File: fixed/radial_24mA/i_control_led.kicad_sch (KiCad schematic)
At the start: 14 parts, among them J1 Conn_01x04, J2 Conn_01x04, Q1 MMBT5551L, U1 TPS61222DCK, U2 LMV321

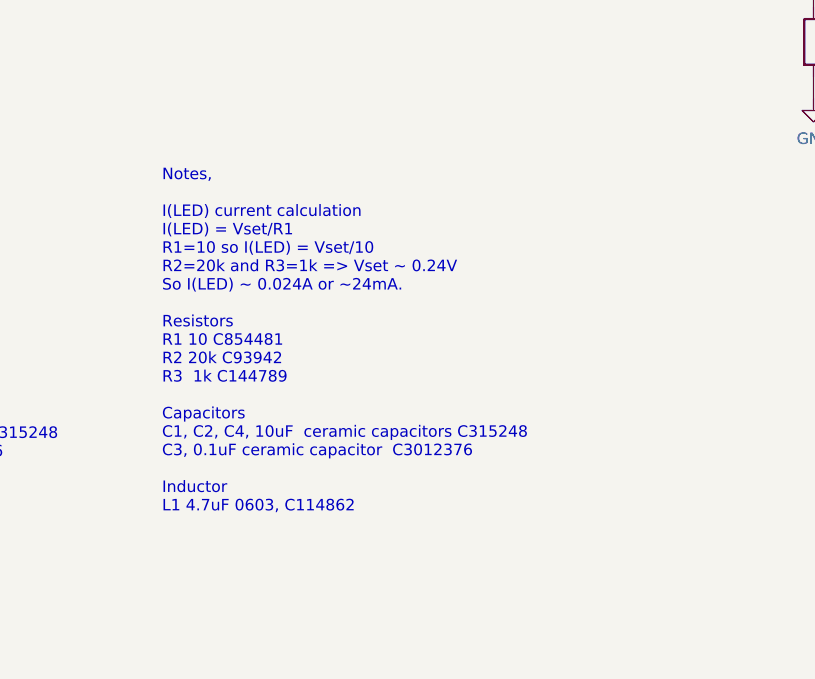
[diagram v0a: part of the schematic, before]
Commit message: Renamed 25mA fixed to 24mA.
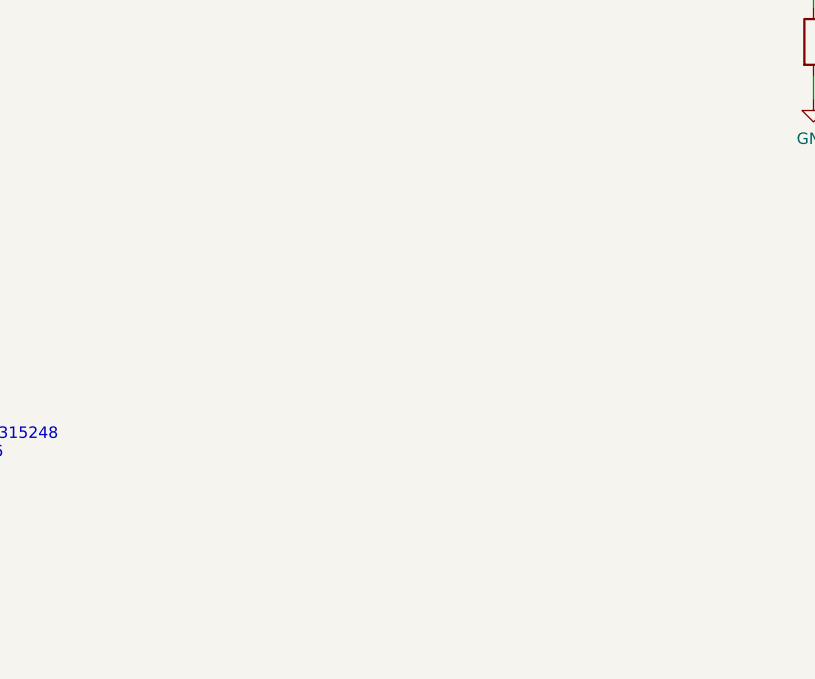
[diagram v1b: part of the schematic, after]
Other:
- note removed: "Notes, I(LED) current calculation I(LED) = Vset/R1 R1=10 so I(LED) = Vset/10 R2=20k and R3=1k => Vset ~ 0.24V So I(LED) ~ 0.024A or ~24mA. Resistors R1 10 C854481 R2 20k C93942 R3 1k C144789 Capacitors C1, C2, C4, 10uF ceramic capacitors C315248 C3, 0.1uF ceramic capacitor C3012376 Inductor L1 4.7uF 0603, C114862"
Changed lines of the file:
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@@
-    (effects (font (size 1.27 1.27)) (justify left bottom))
-  )
-  (text "Notes, \n\nI(LED) current calculation\nI(LED) = Vset/R1\nR1=10 so I(LED) = Vset/10\nR2=20k and R3=1k => Vset ~ 0.24V\nSo I(LED) ~ 0.024A or ~24mA. \n\nResistors\nR1 10 C854481\nR2 20k C93942\nR3  1k C144789\n\nCapacitors\nC1, C2, C4, 10uF  ceramic capacitors C315248\nC3, 0.1uF ceramic capacitor  C3012376\n\nInductor\nL1 4.7uF 0603, C114862\n"
-    (at 84.963 130.302 0)
     (effects (font (size 1.27 1.27)) (justify left bottom))
   )
